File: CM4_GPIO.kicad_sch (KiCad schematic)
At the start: 12 parts, among them J202 Conn_01x02, SW3 TSC015A03518A, U1 RaspberryPi-CM4Lite

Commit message: Weeded out all ERC errors
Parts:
- removed J202: Conn_01x02, symbol Connector_Generic:Conn_01x02
- removed JP3, JP4: Conn_01x02, Connector_PinHeader_2.54mm:PinHeader_1x02_P2.54mm_Vertical, symbol Connector_Generic:Conn_01x02
- removed NT201: NetTie_3_Tee, NetTie:NetTie-3_SMD_Pad0.5mm, symbol Device:NetTie_3_Tee
- removed NT202: NetTie_2, symbol Device:NetTie_2
- removed R1: 10k, Resistor_SMD:R_0402_1005Metric, symbol Device:R_Small
- removed R2: 220R, Resistor_SMD:R_0402_1005Metric, symbol Device:R_Small
- removed SW3: TSC015A03518A, Yellow:SW_SPST_TSC015A03518A, symbol Switch:SW_Push
- removed TP1, TP6, TP7: TestPoint, TestPoint:TestPoint_Pad_D1.0mm, symbol Connector:TestPoint
- removed U1: RaspberryPi-CM4Lite, Yellow:RaspberryPi-CM4, symbol Yellow:RaspberryPi-CM4Lite
- added J202: GPIO, Connector_PinHeader_2.54mm:PinHeader_2x20_P2.54mm_Vertical, symbol Connector_Generic:Conn_02x20_Odd_Even
- added J203: Conn_02x05_Odd_Even, Connector_PinHeader_2.54mm:PinHeader_2x05_P2.54mm_Vertical, symbol Connector_Generic:Conn_02x05_Odd_Even
- added JP202: Conn_01x03_Male, Connector_PinHeader_2.54mm:PinHeader_1x03_P2.54mm_Vertical, symbol Jumper:Jumper_3_Bridged12
- added U201: CM4/5 Module A, Hatlabs:Hirose_DF40_DF40C-100DS-0.4V_2x50_P0.40mm_Vertical, symbol Hatlabs:RaspberryPi-CM45Lite-A
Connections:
- net +5V: now also J202.2 (Pin_2), J202.4 (Pin_4), U201.77 (+5V), U201.79 (+5V), U201.81 (+5V), U201.83 (+5V), U201.85 (+5V), U201.87 (+5V)
- net CAN.CS: now also J202.31 (Pin_31), U201.30 (GPIO6)
- net CAN.INT: now also J202.29 (Pin_29), U201.34 (GPIO5)
- net CAN.SCK: now also J202.23 (Pin_23), U201.38 (GPIO11)
- net CAN.SDI: now also J202.19 (Pin_19), U201.44 (GPIO10)
- net CAN.SDO: now also J202.21 (Pin_21), U201.40 (GPIO9)
- net Console.RXD: now also J202.10 (Pin_10), U201.51 (GPIO15)
- net Console.TXD: now also J202.8 (Pin_8), U201.55 (GPIO14)
- net ETH.LED_GREEN: now also U201.17 (Ethernet_nLED2)
- net ETH.LED_YELLOW: now also U201.15 (Ethernet_nLED3)
- net ETH.TD1+: now also U201.12 (Ethernet_Pair0_P)
- net ETH.TD1-: now also U201.10 (Ethernet_Pair0_N)
- net ETH.TD2+: now also U201.4 (Ethernet_Pair1_P)
- net ETH.TD2-: now also U201.6 (Ethernet_Pair1_N)
- net ETH.TD3+: now also U201.11 (Ethernet_Pair2_P)
- net ETH.TD3-: now also U201.9 (Ethernet_Pair2_N)
- net ETH.TD4+: now also U201.3 (Ethernet_Pair3_P)
- net ETH.TD4-: now also U201.5 (Ethernet_Pair3_N)
- net GND: now also J202.14 (Pin_14), J202.20 (Pin_20), J202.25 (Pin_25), J202.30 (Pin_30), J202.34 (Pin_34), J202.39 (Pin_39), J202.6 (Pin_6), J202.9 (Pin_9), J203.1 (Pin_1), J203.3 (Pin_3), J203.5 (Pin_5), J203.7 (Pin_7), J203.9 (Pin_9), U201.1 (GND), U201.13 (GND), U201.14 (GND), U201.2 (GND), U201.22 (GND), U201.23 (GND), U201.32 (GND), U201.33 (GND), U201.42 (GND), U201.43 (GND), U201.52 (GND), U201.53 (GND), U201.59 (GND), U201.60 (GND), U201.65 (GND), U201.66 (GND), U201.7 (GND), U201.71 (GND), U201.74 (GND), U201.8 (GND), U201.98 (GND)
- net GPIO2: now also J202.3 (Pin_3), U201.58 (GPIO2)
- net GPIO3: now also J202.5 (Pin_5), U201.56 (GPIO3)
- net GPIO4: now also J202.7 (Pin_7), U201.54 (GPIO4)
- net I2C0.SCL: now also U201.80 (SCL0)
- net I2C0.SDA: now also U201.82 (SDA0)
- net SD.CLK: now also U201.57 (SD_CLK)
- net SD.CMD: now also U201.62 (SD_CMD)
- net SD.D0: now also U201.63 (SD_DAT0)
- net SD.D1: now also U201.67 (SD_DAT1)
- net SD.D2: now also U201.69 (SD_DAT2)
- net SD.D3: now also U201.61 (SD_DAT3)
- net SD.PWR: now also U201.75 (SD_PWR_ON)
- net ~{LED_ACT}: now also U201.21 (Pi_nLED_Activity)
- net ~{LED_PWR}: now also U201.95 (PI_LED_nPWR)
- new net CAM_GPIO0: U201.97 (CAM_GPIO0)
- new net CAM_GPIO1: U201.100 (CAM_GPIO1)
- new net CM5_FAN_PWM: JP202.1 (A), U201.19 (Fan_pwm)
- new net CMx_1V8: U201.88 (CM4_1.8V), U201.90 (CM4_1.8V)
- new net CMx_3V3: J202.1 (Pin_1), J202.17 (Pin_17), U201.78 (GPIO_VREF), U201.84 (CM4_3.3V), U201.86 (CM4_3.3V)
- new net EEPROM_nWP: J203.4 (Pin_4), U201.20 (EEPROM_nWP)
- new net FAN_PWM: JP202.2 (C)
- new net FAN_TACHO: U201.16 (Fan_tacho)
- new net GPIO16: J202.36 (Pin_36), U201.29 (GPIO16)
- new net GPIO19: J202.35 (Pin_35), JP202.3 (B), U201.26 (GPIO19)
- new net GPIO20: J202.38 (Pin_38), U201.27 (GPIO20)
- new net GPIO21: J202.40 (Pin_40), U201.25 (GPIO21)
- new net GPIO24: J202.18 (Pin_18), U201.45 (GPIO24)
- new net GPIO25: J202.22 (Pin_22), U201.41 (GPIO25)
- new net GPIO26: J202.37 (Pin_37), U201.24 (GPIO26)
- new net GPIO27: J202.13 (Pin_13), U201.48 (GPIO27)
- new net GPIO7: J202.26 (Pin_26), U201.37 (GPIO7)
- new net GPIO8: J202.24 (Pin_24), U201.39 (GPIO8)
- new net I2C.SCL: J202.16 (Pin_16), U201.47 (GPIO23)
- new net I2C.SDA: J202.15 (Pin_15), U201.46 (GPIO22)
- new net ID.SCL: J202.28 (Pin_28), U201.35 (ID_SC)
- new net ID.SDA: J202.27 (Pin_27), U201.36 (ID_SD)
- new net OTG_ID: J203.8 (Pin_8)
- new net PMIC_ENABLE: J203.10 (Pin_10), U201.99 (PMIC_ENABLE)
- new net PWR_BUTTON: U201.92 (PWR_BUTTON)
- new net Prg.RXD: J202.33 (Pin_33), U201.28 (GPIO13)
- new net Prg.TXD: J202.32 (Pin_32), U201.31 (GPIO12)
- new net RS485.RXD: J202.12 (Pin_12), U201.49 (GPIO18)
- new net RS485.TXD: J202.11 (Pin_11), U201.50 (GPIO17)
- new net SYNC_OUT: J203.6 (Pin_6), U201.18 (Ethernet_SYNC_OUT)
- new net VBAT: U201.76 (VBAT)
- new net nRPIBOOT: J203.2 (Pin_2), U201.93 (nRPIBOOT)
- no-connect marks 17 -> 9
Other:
- note added: "40Way GPIO Header"
- note added: "FAN PWM source selection"
- note added: "Force RPIBOOT = Jumper Pins 1-2"
- company: Nabu Casa -> Hat Labs Oy
- title: Compute Module 4 -> HALPI2

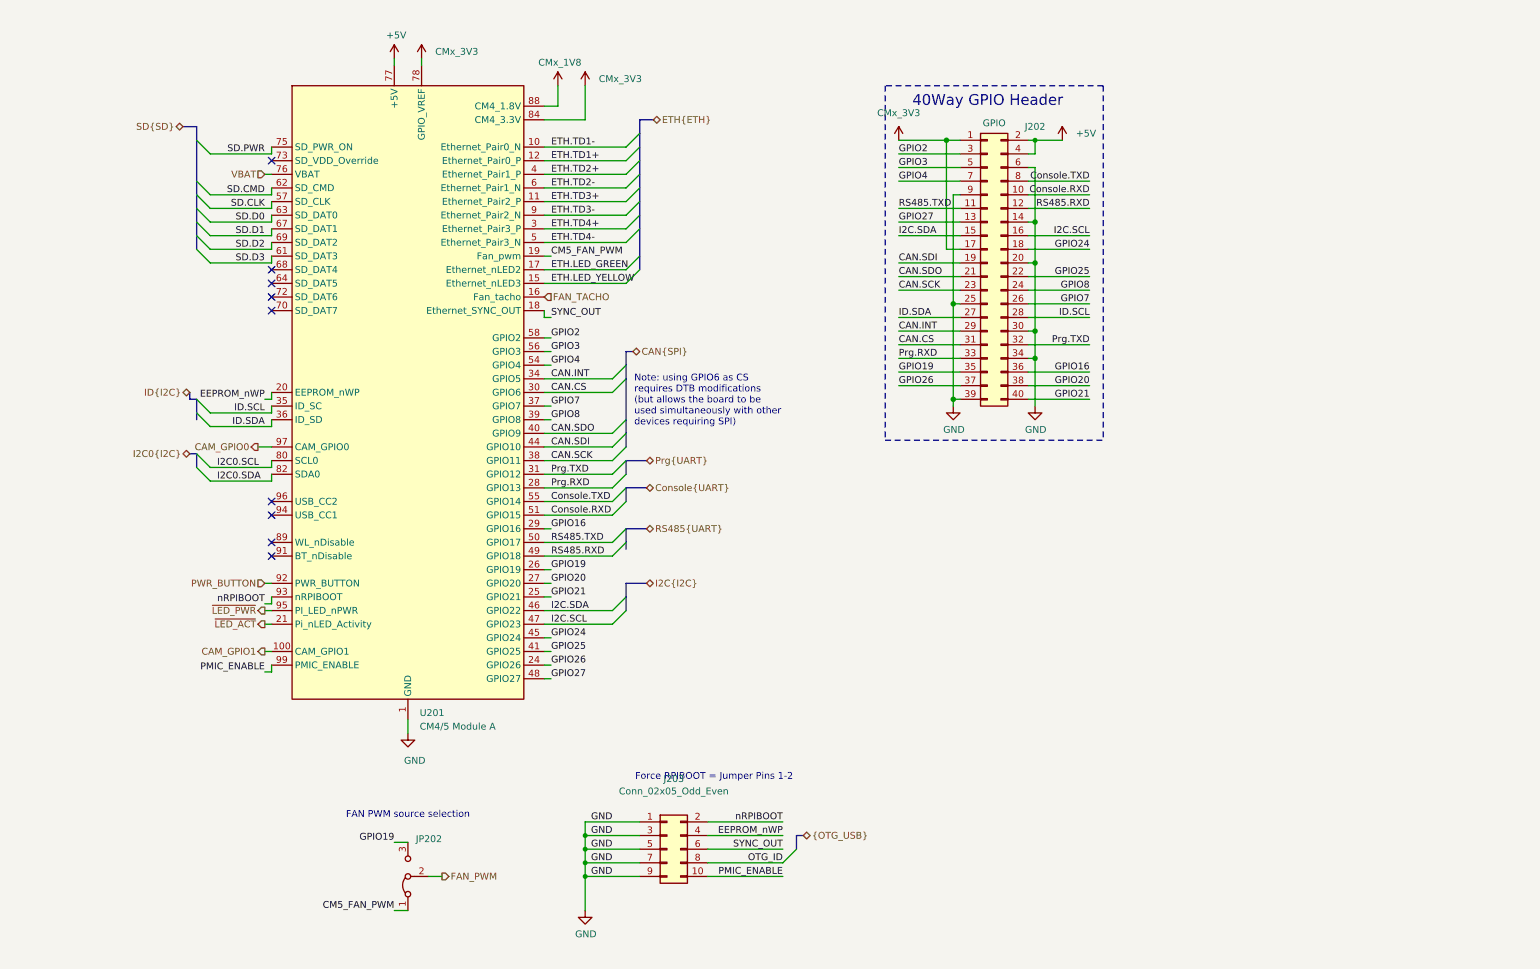
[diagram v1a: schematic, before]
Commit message: Implement ideal diodes for input and LDO power ORing
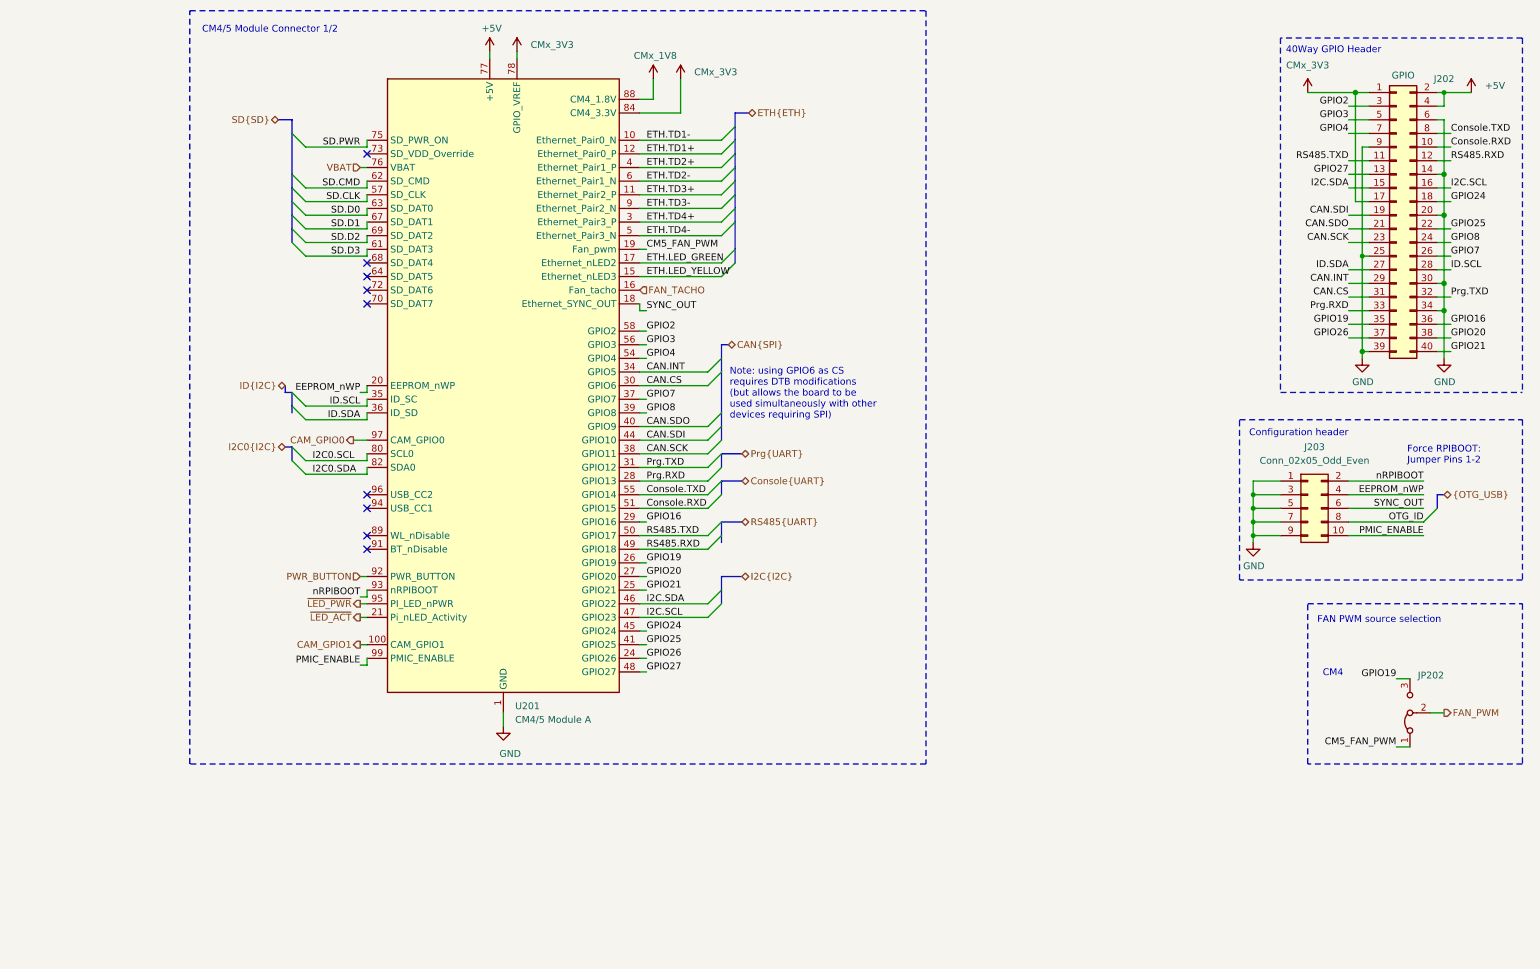
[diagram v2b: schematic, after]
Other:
- note added: "CM4"
- note added: "CM4/5 Module Connector 1/2"
- note added: "Configuration header"
- note added: "Force RPIBOOT: Jumper Pins 1-2"
- note removed: "Force RPIBOOT = Jumper Pins 1-2"
- moved on the sheet: J202, J203, JP202, U201

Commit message: Re-annotate schematics
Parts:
- renumbered J203 to J201, JP202 to JP201
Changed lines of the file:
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@@
 		(on_board yes)
 		(dnp no)
-		(property "Reference" "JP202"
+		(property "Reference" "JP201"
 			(at 256.54 141.6049 90)
 			(effects
@@
 			)
 		)
-		(property "Sim.Enable" ""
-			(at 250.19 148.59 0)
-			(effects
-				(font
-					(size 1.27 1.27)
-				)
-				(hide yes)
-			)
-		)
 		(pin "1"
 		)
@@
 			(project "HALPI2"
 				(path "/abc482bd-3f17-4d35-80db-1da3dcdb5c27/7c248bd3-8232-4777-a40c-eab53460cf85"
-					(reference "JP202")
+					(reference "JP201")
 					(unit 1)
 				)
@@
 		(on_board yes)
 		(dnp no)
-		(property "Reference" "#PWR0210"
+		(property "Reference" "#PWR0209"
 			(at 256.54 88.9 0)
 			(effects
@@
 			(project "HALPI2"
 				(path "/abc482bd-3f17-4d35-80db-1da3dcdb5c27/7c248bd3-8232-4777-a40c-eab53460cf85"
-					(reference "#PWR0210")
+					(reference "#PWR0209")
 					(unit 1)
 				)
@@
 		(dnp no)
 		(fields_autoplaced yes)
-		(property "Reference" "#PWR0211"
+		(property "Reference" "#PWR0210"
 			(at 261.62 36.83 0)
 			(effects
@@
 			(project "HALPI2"
 				(path "/abc482bd-3f17-4d35-80db-1da3dcdb5c27/7c248bd3-8232-4777-a40c-eab53460cf85"
-					(reference "#PWR0211")
+					(reference "#PWR0210")
 					(unit 1)
 				)
@@
 			)
 		)
-		(property "Sim.Enable" ""
-			(at 247.65 55.88 0)
-			(effects
-				(font
-					(size 1.27 1.27)
-				)
-				(hide yes)
-			)
-		)
 		(pin "1"
 		)
@@
 			)
 		)
-		(property "Sim.Enable" ""
-			(at 81.28 87.63 0)
-			(effects
-				(font
-					(size 1.27 1.27)
-				)
-				(hide yes)
-			)
-		)
 		(pin "28"
 		)
@@
 		(dnp no)
 		(fields_autoplaced yes)
-		(property "Reference" "#PWR0208"
+		(property "Reference" "#PWR0207"
 			(at 231.14 36.83 0)
 			(effects
@@
 			(project "HALPI2"
 				(path "/abc482bd-3f17-4d35-80db-1da3dcdb5c27/7c248bd3-8232-4777-a40c-eab53460cf85"
-					(reference "#PWR0208")
+					(reference "#PWR0207")
 					(unit 1)
 				)
@@
 		(dnp no)
 		(fields_autoplaced yes)
-		(property "Reference" "J203"
+		(property "Reference" "J201"
 			(at 232.41 99.06 0)
 			(effects
@@
 			)
 		)
-		(property "Sim.Enable" ""
-			(at 231.14 110.49 0)
-			(effects
-				(font
-					(size 1.27 1.27)
-				)
-				(hide yes)
-			)
-		)
 		(pin "1"
 		)
@@
 			(project "HALPI2"
 				(path "/abc482bd-3f17-4d35-80db-1da3dcdb5c27/7c248bd3-8232-4777-a40c-eab53460cf85"
-					(reference "J203")
+					(reference "J201")
 					(unit 1)
 				)
@@
 		(on_board yes)
 		(dnp no)
-		(property "Reference" "#PWR0209"
+		(property "Reference" "#PWR0208"
 			(at 241.3 88.9 0)
 			(effects
@@
 			(project "HALPI2"
 				(path "/abc482bd-3f17-4d35-80db-1da3dcdb5c27/7c248bd3-8232-4777-a40c-eab53460cf85"
-					(reference "#PWR0209")
+					(reference "#PWR0208")
 					(unit 1)
 				)
@@
 		(on_board yes)
 		(dnp no)
-		(property "Reference" "#PWR0212"
+		(property "Reference" "#PWR0206"
 			(at 220.98 123.19 0)
 			(effects
@@
 			(project "HALPI2"
 				(path "/abc482bd-3f17-4d35-80db-1da3dcdb5c27/7c248bd3-8232-4777-a40c-eab53460cf85"
-					(reference "#PWR0212")
-					(unit 1)
-				)
+					(reference "#PWR0206")
+					(unit 1)
+				)

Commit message: Implement a USB3 hub
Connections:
- net CMx_3V3 renamed +3.3VCMx
- net +3.3VCMx: no longer J202.1 (Pin_1), J202.17 (Pin_17)
- net OTG_ID: no longer names the net of J201.8 (Pin_8)
- new net +3.3V: J202.1 (Pin_1), J202.17 (Pin_17)
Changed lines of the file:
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@@
 	)
 	(bus_entry
-		(at 255.27 110.49)
-		(size -2.54 2.54)
-		(stroke
-			(width 0.1524)
-			(type solid)
-		)
-	)
-	(bus_entry
 		(at 121.92 67.31)
 		(size 2.54 -2.54)
@@
 		)
 	)
-	(bus
-		(pts
-			(xy 255.27 107.95) (xy 255.27 110.49)
-		)
-		(stroke
-			(width 0)
-			(type solid)
-		)
-	)
 	(wire
 		(pts
@@
 		)
 	)
-	(bus
-		(pts
-			(xy 256.54 107.95) (xy 255.27 107.95)
-		)
-		(stroke
-			(width 0)
-			(type solid)
-		)
-	)
 	(wire
 		(pts
@@
 		)
 	)
-	(label "OTG_ID"
-		(at 252.73 113.03 180)
-		(fields_autoplaced yes)
-		(effects
-			(font
-				(size 1.27 1.27)
-			)
-			(justify right bottom)
-		)
-	)
 	(label "CAN.SCK"
 		(at 238.76 60.96 180)
@@
 		)
 	)
-	(hierarchical_label "{OTG_USB}"
-		(shape bidirectional)
-		(at 256.54 107.95 0)
-		(fields_autoplaced yes)
-		(effects
-			(font
-				(size 1.27 1.27)
-			)
-			(justify left)
-		)
-	)
 	(hierarchical_label "CAM_GPIO1"
 		(shape output)
@@
 	)
 	(symbol
-		(lib_id "power:+3V3")
+		(lib_id "Hatlabs:+3.3VCMx")
 		(at 114.3 30.48 0)
 		(unit 1)
@@
 			)
 		)
-		(property "Value" "CMx_3V3"
+		(property "Value" "+3.3VCMx"
 			(at 116.84 29.2099 0)
 			(effects
@@
 			)
 		)
-		(property "Description" "Power symbol creates a global label with name \"+3V3\""
+		(property "Description" "Power symbol driven by the CMx module +3.3V output"
 			(at 114.3 30.48 0)
 			(effects
@@
 	)
 	(symbol
-		(lib_id "power:+3V3")
+		(lib_id "Hatlabs:+3.3VCMx")
 		(at 83.82 25.4 0)
 		(unit 1)
@@
 			)
 		)
-		(property "Value" "CMx_3V3"
+		(property "Value" "+3.3VCMx"
 			(at 86.36 24.1299 0)
 			(effects
@@
 			)
 		)
-		(property "Description" "Power symbol creates a global label with name \"+3V3\""
+		(property "Description" "Power symbol driven by the CMx module +3.3V output"
 			(at 83.82 25.4 0)
 			(effects
@@
 	)
 	(symbol
-		(lib_id "power:+3V3")
+		(lib_id "power:+3.3V")
 		(at 231.14 33.02 0)
 		(unit 1)
@@
 			)
 		)
-		(property "Value" "CMx_3V3"
+		(property "Value" "+3.3V"
 			(at 231.14 27.94 0)
 			(effects
@@
 			)
 		)
-		(property "Description" "Power symbol creates a global label with name \"+3V3\""
+		(property "Description" "Power symbol creates a global label with name \"+3.3V\""
 			(at 231.14 33.02 0)
 			(effects
@@
 		)
 		(instances
-			(project "HALPI2"
+			(project ""
 				(path "/abc482bd-3f17-4d35-80db-1da3dcdb5c27/7c248bd3-8232-4777-a40c-eab53460cf85"
 					(reference "#PWR0207")

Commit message: Partial trace layout, kick-ass custom rules
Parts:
- added H201: HAT outline, Hatlabs:RPi_HAT_Outline, symbol Mechanical:MountingHole
- renumbered J202 to J201, J201 to J202
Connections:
- no-connect marks 9 -> 10
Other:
- added sheet Fan Connectors (fan_connectors.kicad_sch)

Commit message: A big part of layout and routing done
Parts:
- J202: Part Description PinHeader_2x05_P2.54mm_Vertical -> (none)
- JP201: Manufacturer Adam Tech -> (none); PartNumber PH1-03-UA -> (none)
- U201: Component Class (none) -> fine_pitch

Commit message: Route more traces
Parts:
- added R304: 0R, Resistor_SMD:R_0805_2012Metric, symbol Device:R
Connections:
- net GPIO26 is gone; now on net CAN.INT: J201.37 (Pin_37), U201.24 (GPIO26)
- net CAN.CS: now also R304.2; no longer J201.31 (Pin_31), U201.30 (GPIO6)
- net CAN.INT: no longer J201.29 (Pin_29), U201.34 (GPIO5)
- net GPIO19: no longer JP201.3 (B)
- net GPIO2 renamed I2C1.SDA
- net GPIO24 renamed RS485.~{EN}
- net GPIO3 renamed I2C1.SCL
- net I2C.SCL renamed GPIO23
- net I2C.SDA renamed GPIO22
- net GPIO22: now also JP201.3 (B)
- new net GPIO5: J201.29 (Pin_29), U201.34 (GPIO5)
- new net GPIO6: J201.31 (Pin_31), R304.1, U201.30 (GPIO6)
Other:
- note added: "FAN PWM destination selection"
- note removed: "FAN PWM source selection"
- moved on the sheet: H201
